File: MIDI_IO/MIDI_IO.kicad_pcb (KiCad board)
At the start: 2 copper layers, 50 x 40 mm, 21 parts, among them J1 Conn_01x04, U1 6N138

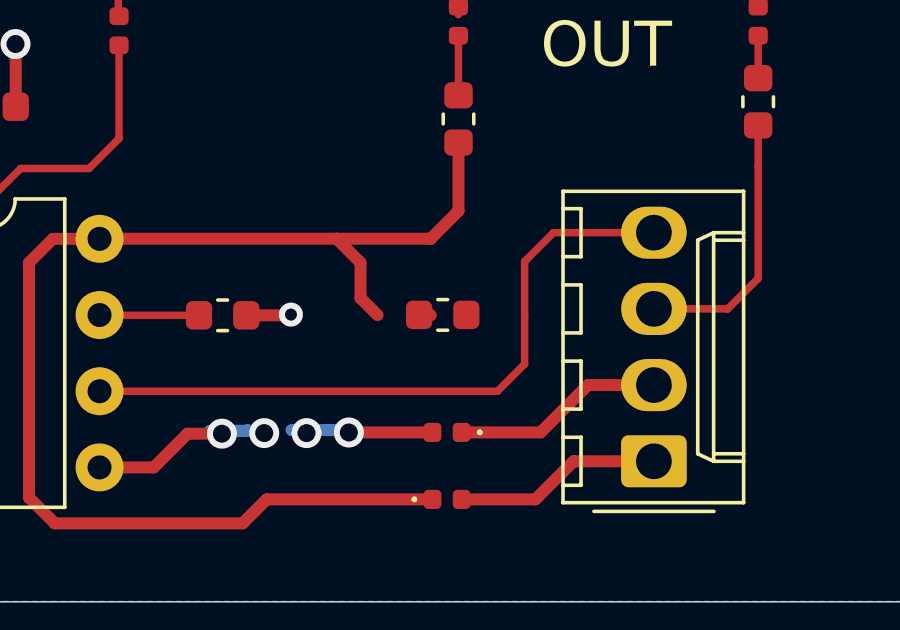
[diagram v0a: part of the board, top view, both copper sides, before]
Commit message: Fixes naming for MIDI IO board
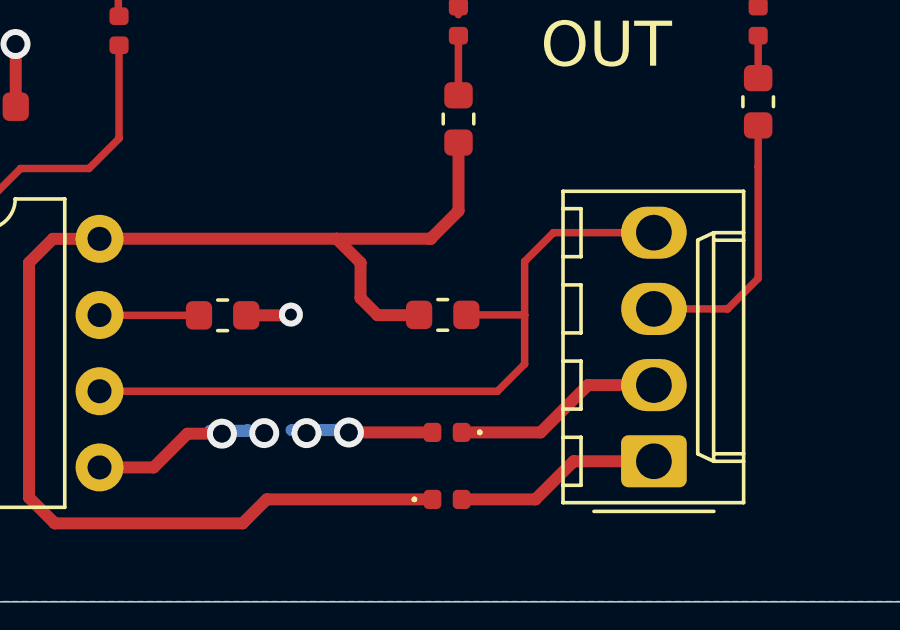
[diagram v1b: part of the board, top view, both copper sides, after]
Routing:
- net RX: track 22.7 -> 24.6 mm
- net +5V: track 42.0 -> 43.4 mm
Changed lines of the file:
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@@
     (thickness 1.6)
     (drawings 8)
-    (tracks 87)
+    (tracks 90)
     (zones 0)
     (modules 21)
@@
   (segment (start 44.71596 41.03534) (end 43.78 41.9713) (width 0.4) (layer F.Cu) (net 17))
   (segment (start 44.71596 38.75622) (end 44.71596 41.03534) (width 0.4) (layer F.Cu) (net 17))
-  (segment (start 43.78 44.4975) (end 43.7925 44.51) (width 0.4) (layer F.Cu) (net 17))
   (segment (start 31.195 41.965) (end 32.7508 41.965) (width 0.4) (layer F.Cu) (net 17))
   (segment (start 37.52 51.45) (end 31.26 51.45) (width 0.4) (layer F.Cu) (net 17))
@@
   (segment (start 42.02 44.51) (end 41.45 43.94) (width 0.4) (layer F.Cu) (net 17))
   (segment (start 43.85 50.65) (end 38.32 50.65) (width 0.4) (layer F.Cu) (net 17))
+  (segment (start 43.3925 44.51) (end 43.4025 44.5) (width 0.4) (layer F.Cu) (net 17))
+  (segment (start 42.02 44.51) (end 43.3925 44.51) (width 0.4) (layer F.Cu) (net 17))
   (segment (start 46.92 44.51) (end 46.92 46.14) (width 0.25) (layer F.Cu) (net 18))
   (segment (start 46.015 47.045) (end 32.7508 47.045) (width 0.25) (layer F.Cu) (net 18))
@@
   (segment (start 46.92 44.51) (end 46.92 42.72) (width 0.25) (layer F.Cu) (net 18))
   (segment (start 46.92 42.72) (end 47.88 41.76) (width 0.25) (layer F.Cu) (net 18))
+  (segment (start 46.91 44.5) (end 46.92 44.51) (width 0.25) (layer F.Cu) (net 18))
+  (segment (start 44.9775 44.5) (end 46.91 44.5) (width 0.25) (layer F.Cu) (net 18))
   (segment (start 32.7608 44.515) (end 32.7508 44.505) (width 0.25) (layer F.Cu) (net 19) (status 30))
   (segment (start 36.066 44.515) (end 32.7608 44.515) (width 0.25) (layer F.Cu) (net 19) (status 30))

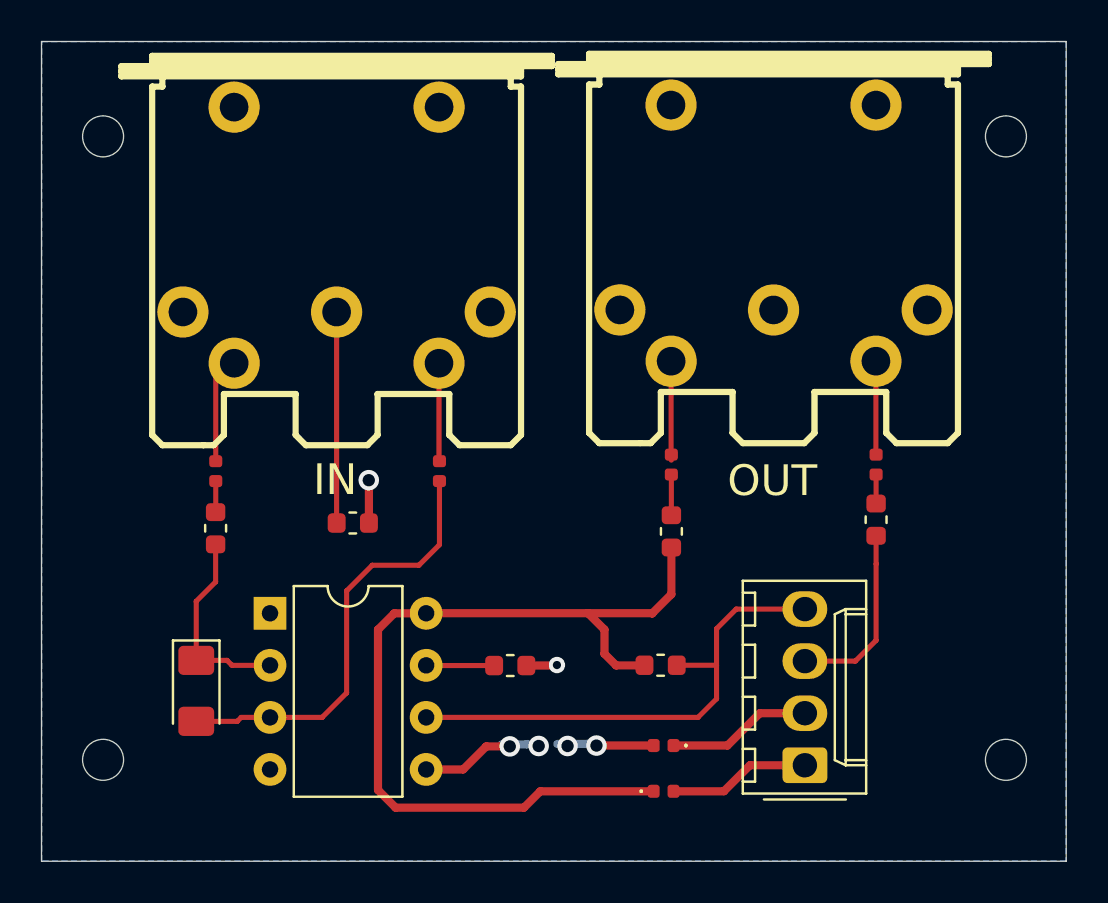
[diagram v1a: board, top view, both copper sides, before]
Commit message: Improves MIDI shield
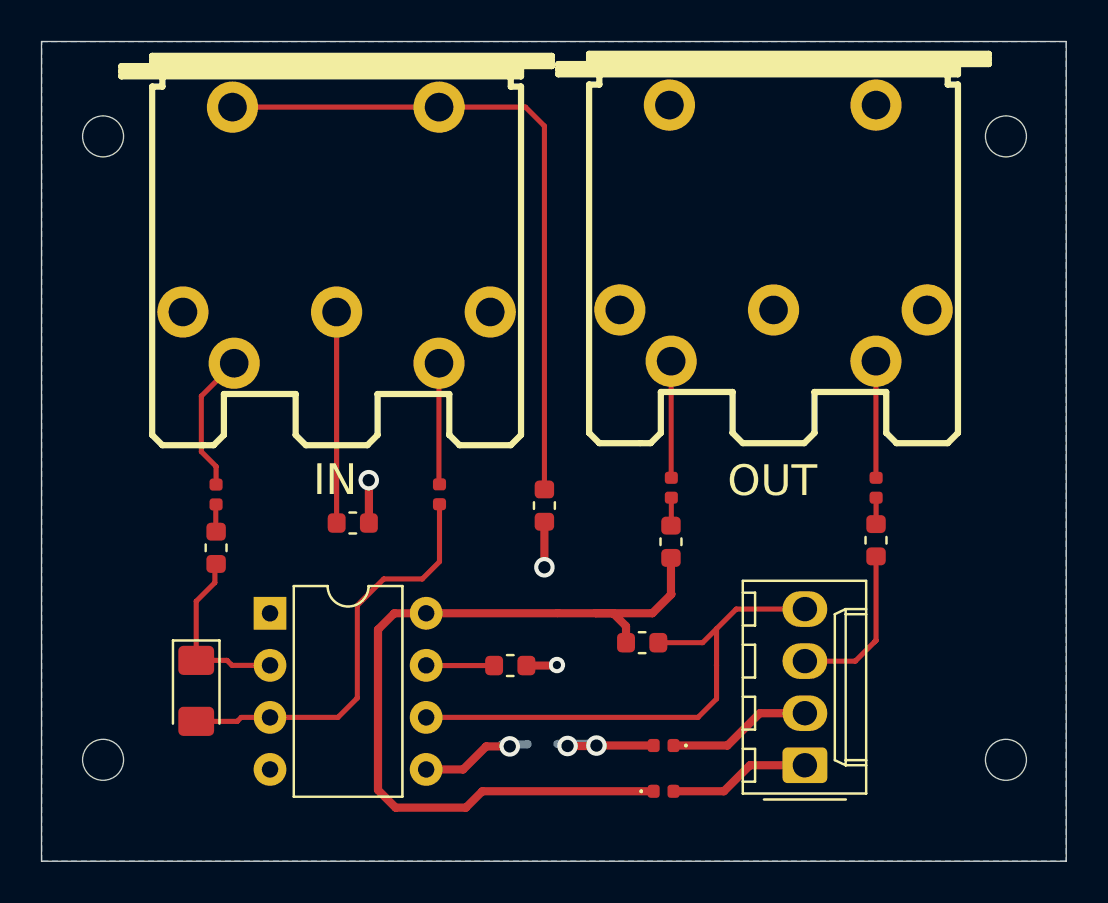
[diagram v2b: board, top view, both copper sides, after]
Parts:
- added C2: 0.1uF, Capacitor_SMD:C_0603_1608Metric, F.Cu at (38.5, 36.7)
- C1: value 0.1 uF -> 0.1uF
- J_IN_1, J_OUT_1: value DIN-5_180degree -> DIN-5_180degree_JS; footprint w_conn_av:din-5 -> MIDI_IO:din-5-shielded
- moved R4 1.42 mm to (43.3, 43.4)
- moved FB3 1.14 mm to (22.5, 36.2)
- moved FB1 1.13 mm to (54.7, 35.8)
- moved FB2 1.13 mm to (44.7, 35.8)
- moved FB4 1.13 mm to (33.4, 36.2)
- moved R1 1.00 mm to (54.7, 38.4)
- moved R3 0.95 mm to (22.5, 38.8)
- moved R2 0.51 mm to (44.7, 38.5)
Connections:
- net Net-(C1-Pad1) renamed IN_SH
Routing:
- net IN_SH_OUT: track 0.00 -> 33.3 mm
- net GND: track 13.7 -> 17.3 mm
- net Net-(FB3-Pad2): track 4.80 -> 6.88 mm
- net +5V: track 43.4 -> 41.3 mm
- net RX: track 24.6 -> 25.8 mm
- net Net-(FB1-Pad1): track 4.56 -> 5.69 mm
- net Net-(FB4-Pad2): track 4.79 -> 5.92 mm
- net Net-(FB2-Pad2): track 4.58 -> 5.70 mm
- net Net-(D1-Pad1): track 9.75 -> 8.79 mm
- net TX: track 9.00 -> 8.07 mm
- net Net-(D1-Pad2): track 21.5 -> 20.6 mm
- net Net-(FB2-Pad1): track 1.99 -> 1.37 mm

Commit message: Updates MIDI-IO board to a last state
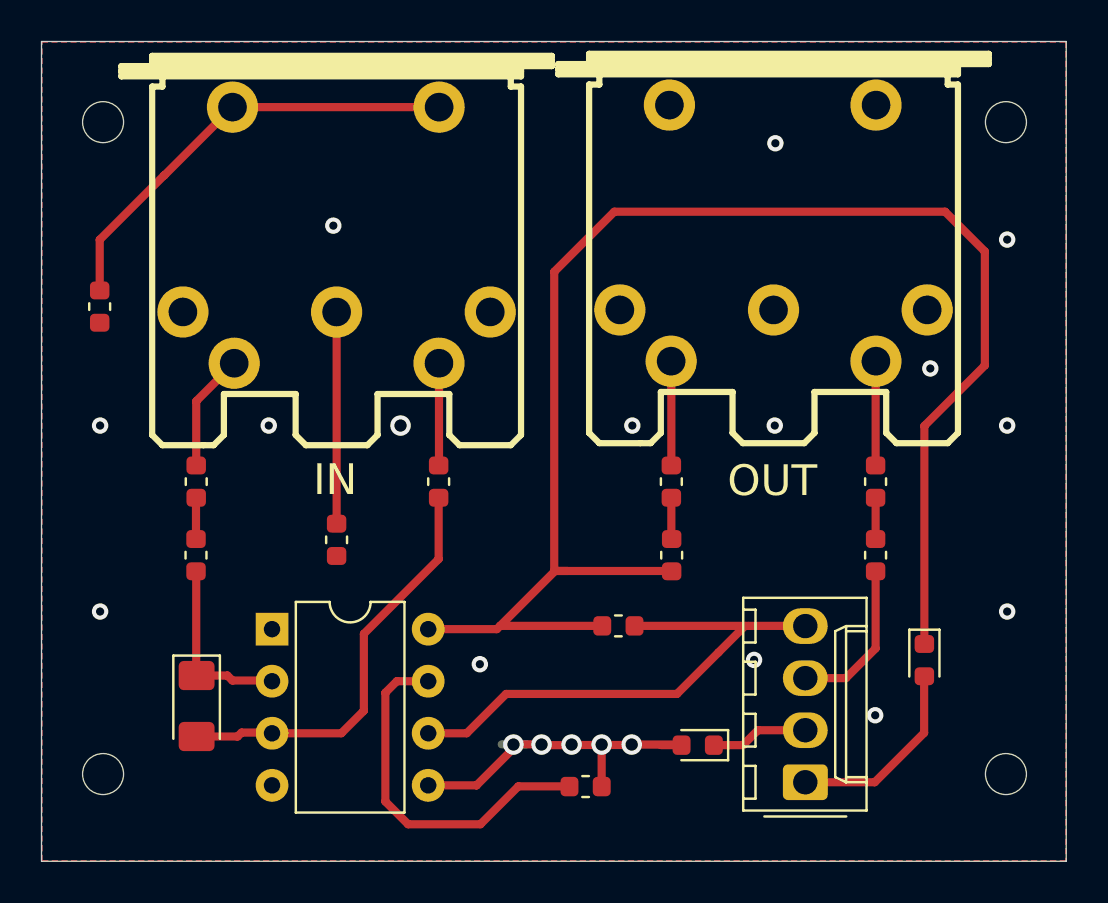
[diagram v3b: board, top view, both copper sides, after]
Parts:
- added svg2mod: G***, Logo:Grid_logo, B.Cu at (42.0, 40.1)
- D2, D3: footprint Diode_SMD:D_0402_1005Metric -> Diode_SMD:D_0603_1608Metric
- FB1, FB2, FB3, FB4: footprint Inductor_SMD:L_0402_1005Metric -> Inductor_SMD:L_0603_1608Metric
- moved C2 23.8 mm to (16.8, 27.0)
- moved D2 14.2 mm to (57.1, 44.2), turned to 270 degrees
- moved R5 6.96 mm to (40.5, 50.4)
- moved D3 1.67 mm to (46.0, 48.4)
- moved R4 1.42 mm to (42.1, 42.6)
- moved FB3 1.16 mm to (21.5, 35.5)
- moved C1 1.14 mm to (28.4, 38.4), turned to 270 degrees
- moved R3 1.04 mm to (21.5, 39.1)
- moved J1 0.83 mm to (51.2, 50.2)
- moved U1 0.78 mm to (25.2, 42.7)
- moved D1 0.74 mm to (21.6, 46.5)
- moved R1 0.73 mm to (54.7, 39.1)
- moved H1 0.70 mm to (17.0, 18.0)
- moved H3 0.70 mm to (61.0, 18.0)
- moved H2 0.70 mm to (17.0, 49.8)
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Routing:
- net +5V: track 41.3 -> 76.7 mm
- net Net-(R5-Pad1): track 3.32 -> 17.8 mm
- net IN_SH_OUT: track 33.3 -> 21.7 mm
- net Net-(D2-Pad2): track 6.94 -> 9.56 mm
- net Net-(D3-Pad1): track 7.06 -> 4.78 mm
- net Net-(FB3-Pad2): track 6.88 -> 5.76 mm
- net Net-(FB4-Pad2): track 5.92 -> 5.00 mm
- net Net-(FB3-Pad1): track 1.32 -> 2.02 mm
- net Net-(FB1-Pad2): track 1.32 -> 2.02 mm
- net Net-(FB2-Pad1): track 1.37 -> 2.02 mm
- net Net-(FB2-Pad2): track 5.70 -> 5.09 mm
- net Net-(FB1-Pad1): track 5.69 -> 5.10 mm
- net GND: track 17.3 -> 17.5 mm, vias 6 -> 20
- added copper zone on F.Cu, net GND
